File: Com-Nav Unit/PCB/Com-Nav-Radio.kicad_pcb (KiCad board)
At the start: 2 copper layers, 147 x 45 mm, 84 parts, among them J1 GT-USB-7055, Q10 SS8550, Q11 SS8550, Q12 SS8550, Q13 SS8550, Q14 SS8550, Q15 SS8550, Q16 SS8550, Q2 SS8550, Q3 SS8550, Q4 SS8550, Q5 SS8550, Q6 SS8550, Q7 SS8550, Q8 SS8550, Q9 SS8550, SW1 EC12D1524403, SW2 EC12E1240301, SW3 EC12D1524403, SW4 EC12E1240301, U1 STM32F411CEUx, U10 FJ2352BH, U11 FJ2352BH, U12 FJ2352BH, U13 FJ2352BH, U14 FJ2352BH, U2 74HC595, U3 74HC595, U4 XC6206P332MR, U5 FJ2352BH, U6 FJ2352BH, U7 FJ2352BH, U8 FJ2352BH, U9 FJ2352BH, Y2 25 MHz

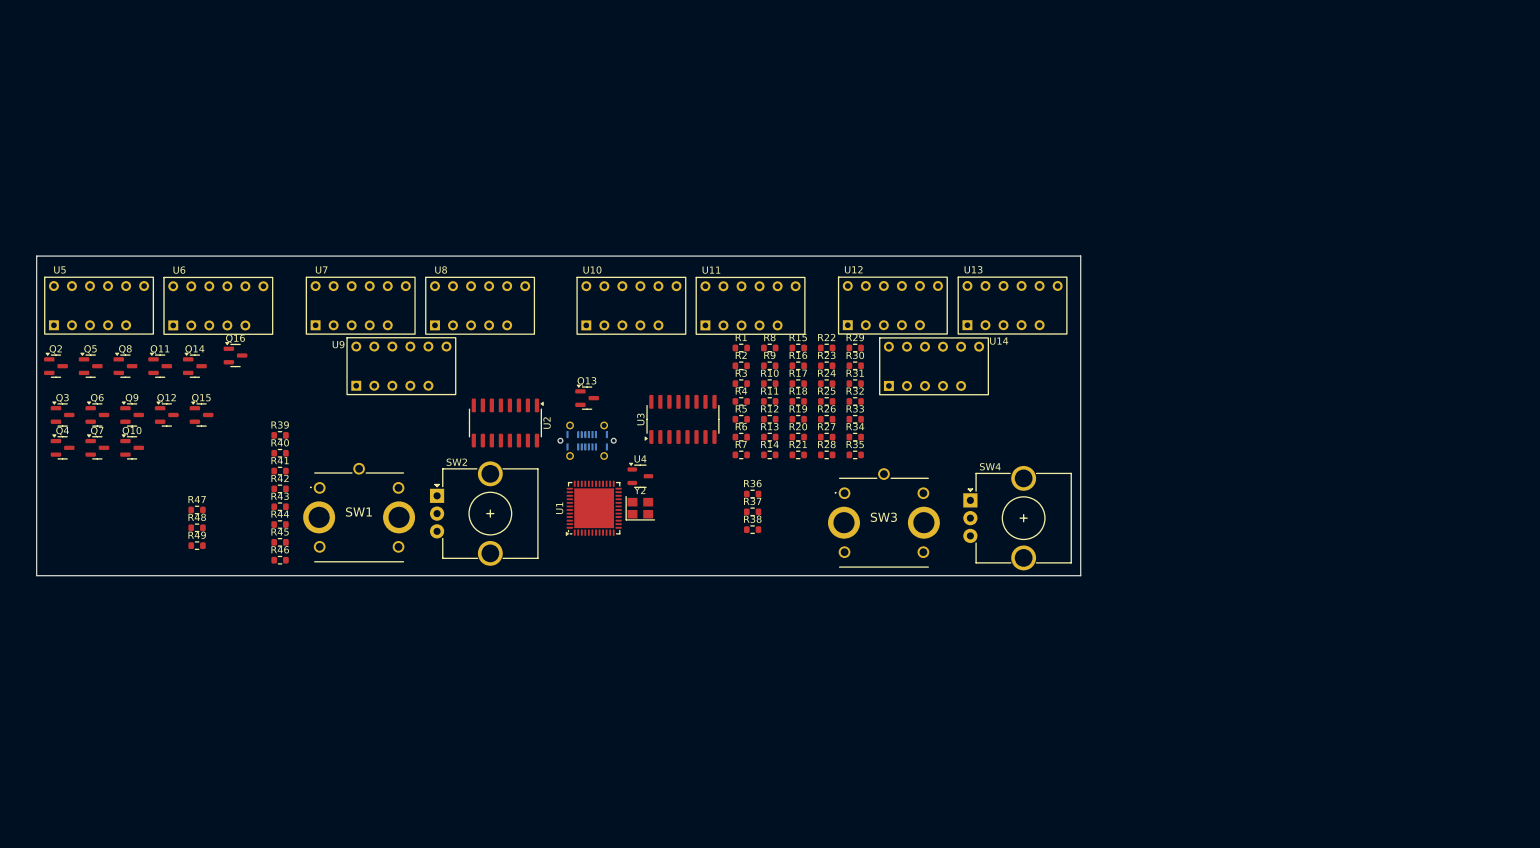
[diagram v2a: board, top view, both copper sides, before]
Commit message: PCB - Changed to common cathode with 2 more shift reg
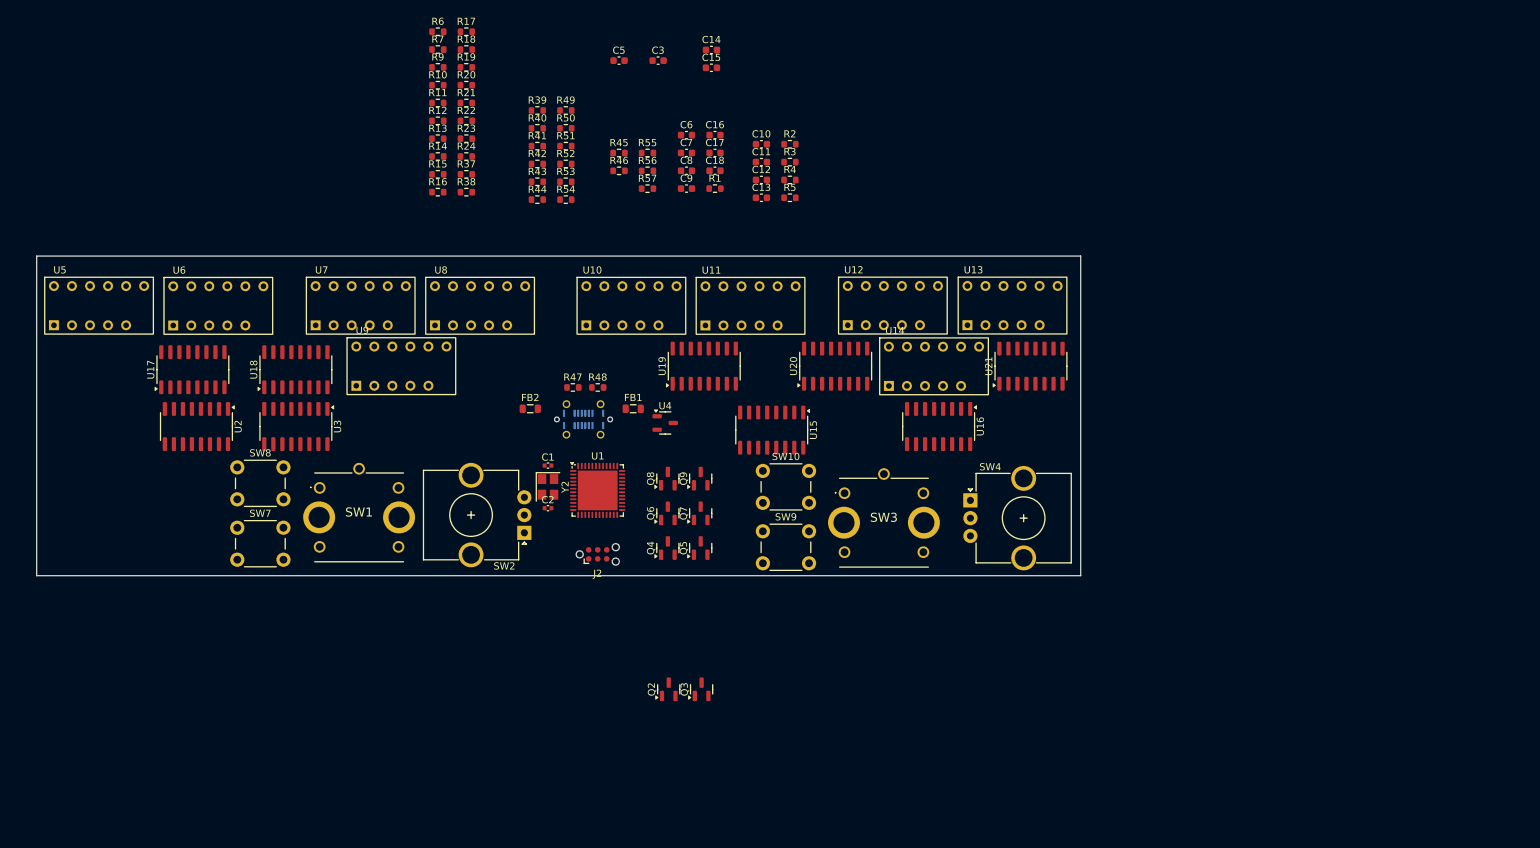
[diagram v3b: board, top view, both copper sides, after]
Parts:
- removed Q10, Q11, Q12, Q13, Q14, Q15, Q16: SS8550, Package_TO_SOT_SMD:SOT-23
- removed R25, R26, R27, R28, R29, R30, R31, R32, R33, R34, R35: 100, Resistor_SMD:R_0603_1608Metric
- removed R36: 0, Resistor_SMD:R_0603_1608Metric
- removed R8: 10k, Resistor_SMD:R_0603_1608Metric
- added C1: 10p, Capacitor_SMD:C_0402_1005Metric, F.Cu at (150.5, 106.5)
- added C10: 100n, Capacitor_SMD:C_0603_1608Metric, F.Cu at (180.6, 61.3)
- added C11: 100n, Capacitor_SMD:C_0603_1608Metric, F.Cu at (180.6, 63.8)
- added C12: 100n, Capacitor_SMD:C_0603_1608Metric, F.Cu at (180.6, 66.3)
- added C13: 100n, Capacitor_SMD:C_0603_1608Metric, F.Cu at (180.6, 68.8)
- added C14: 2.2u, Capacitor_SMD:C_0603_1608Metric, F.Cu at (173.5, 48.0)
- added C15: 100n, Capacitor_SMD:C_0603_1608Metric, F.Cu at (173.5, 50.5)
- added C16: 100n, Capacitor_SMD:C_0603_1608Metric, F.Cu at (174.0, 60.0)
- added C17: 2.2u, Capacitor_SMD:C_0603_1608Metric, F.Cu at (174.0, 62.5)
- added C18: 2.2u, Capacitor_SMD:C_0603_1608Metric, F.Cu at (174.0, 65.0)
- added C2: 10p, Capacitor_SMD:C_0402_1005Metric, F.Cu at (150.5, 112.5)
- added C3: 2.2u, Capacitor_SMD:C_0603_1608Metric, F.Cu at (166.0, 49.5)
- added C5: 2.2u, Capacitor_SMD:C_0603_1608Metric, F.Cu at (160.5, 49.5)
- added C6: 100n, Capacitor_SMD:C_0603_1608Metric, F.Cu at (170.0, 60.0)
- added C7: 2.2u, Capacitor_SMD:C_0603_1608Metric, F.Cu at (170.0, 62.5)
- added C8: 100n, Capacitor_SMD:C_0603_1608Metric, F.Cu at (170.0, 65.0)
- added C9: 100n, Capacitor_SMD:C_0603_1608Metric, F.Cu at (170.0, 67.5)
- added FB1: GZ2012D601TF, Inductor_SMD:L_0805_2012Metric, F.Cu at (162.5, 98.5)
- added FB2: GZ2012D601TF, Inductor_SMD:L_0805_2012Metric, F.Cu at (148.0, 98.5)
- added J2: TC2030, Connector:Tag-Connect_TC2030-IDC-NL_2x03_P1.27mm_Vertical, F.Cu at (157.5, 119.0)
- added R50: 10k, Resistor_SMD:R_0603_1608Metric, F.Cu at (153.0, 59.0)
- added R51: 10k, Resistor_SMD:R_0603_1608Metric, F.Cu at (153.0, 61.5)
- added R52: 10k, Resistor_SMD:R_0603_1608Metric, F.Cu at (153.0, 64.0)
- added R53: 10k, Resistor_SMD:R_0603_1608Metric, F.Cu at (153.0, 66.5)
- added R54: 10k, Resistor_SMD:R_0603_1608Metric, F.Cu at (153.0, 69.0)
- added R55: 10k, Resistor_SMD:R_0603_1608Metric, F.Cu at (164.5, 62.5)
- added R56: 10k, Resistor_SMD:R_0603_1608Metric, F.Cu at (164.5, 65.0)
- added R57: 10k, Resistor_SMD:R_0603_1608Metric, F.Cu at (164.5, 67.5)
- added SW10: SW_Push, Button_Switch_THT:SW_PUSH_6mm, F.Cu at (180.8, 107.2)
- added SW7: SW_Push, Button_Switch_THT:SW_PUSH_6mm, F.Cu at (106.8, 115.2)
- added SW8: SW_Push, Button_Switch_THT:SW_PUSH_6mm, F.Cu at (106.8, 106.8)
- added SW9: SW_Push, Button_Switch_THT:SW_PUSH_6mm, F.Cu at (180.8, 115.8)
- added U15: 74HC595, Package_SO:SOIC-16_3.9x9.9mm_P1.27mm, F.Cu at (182.0, 101.5)
- added U16: 74HC595, Package_SO:SOIC-16_3.9x9.9mm_P1.27mm, F.Cu at (205.5, 101.0)
- added U17: ULN2003A, Package_SO:SOIC-16_3.9x9.9mm_P1.27mm, F.Cu at (100.5, 93.0)
- added U18: ULN2003A, Package_SO:SOIC-16_3.9x9.9mm_P1.27mm, F.Cu at (115.0, 93.0)
- added U19: ULN2003A, Package_SO:SOIC-16_3.9x9.9mm_P1.27mm, F.Cu at (172.5, 92.5)
- added U20: ULN2003A, Package_SO:SOIC-16_3.9x9.9mm_P1.27mm, F.Cu at (191.0, 92.5)
- added U21: ULN2003A, Package_SO:SOIC-16_3.9x9.9mm_P1.27mm, F.Cu at (218.5, 92.5)
- Q2, Q3, Q4, Q5, Q6, Q7, Q8, Q9: value SS8550 -> AO3401A
- R10, R11, R12, R13, R14, R15, R16, R17, R18, R19, R20, R9: value 10k -> 100
- U10, U11, U12, U13, U14, U5, U6, U7, U8, U9: value FJ2352BH -> FJ2352; footprint Custom_7seg:FJ2352BH -> Custom_7seg:FJ2352
- moved Q3 97.9 mm to (172.1, 138.0), turned to 90 degrees
- moved Q2 97.5 mm to (167.5, 138.0), turned to 90 degrees
- moved Q5 89.6 mm to (172.0, 118.1), turned to 90 degrees
- moved Q4 86.4 mm to (167.4, 118.1), turned to 90 degrees
- moved Q7 85.5 mm to (172.0, 113.2), turned to 90 degrees
- moved Q6 81.5 mm to (167.4, 113.2), turned to 90 degrees
- moved Q9 80.6 mm to (172.0, 108.3), turned to 90 degrees
- moved R49 80.3 mm to (153.0, 56.5)
- moved Q8 78.0 mm to (167.4, 108.3), turned to 90 degrees
- moved R45 72.7 mm to (160.5, 62.5)
- moved R46 72.7 mm to (160.5, 65.0)
- moved R6 71.3 mm to (135.0, 45.4)
- moved R7 71.3 mm to (135.0, 47.9)
- moved R19 68.1 mm to (139.0, 50.4)
- moved R17 68.1 mm to (139.0, 45.4)
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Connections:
- J1 pad A4: +5V -> Net-(FB1-Pad1)
- J1 pad A9: +5V -> Net-(FB1-Pad1)
- J1 pad B4: +5V -> Net-(FB1-Pad1)
- J1 pad B9: +5V -> Net-(FB1-Pad1)
- Q2 pad 1: Net-(Q2-B) -> Net-(Q2-G)
- Q2 pad 2: +5V -> Net-(Q2-S)
- Q2 pad 3: /DIG.1 -> Net-(Q2-D)
- Q3 pad 1: Net-(Q3-B) -> Net-(Q3-G)
- Q3 pad 2: +5V -> Net-(Q2-S)
- Q3 pad 3: /DIG2 -> Net-(Q3-D)
- Q4 pad 1: Net-(Q4-B) -> Net-(Q4-G)
- Q4 pad 2: +5V -> Net-(Q2-S)
- Q4 pad 3: /DIG3 -> Net-(Q4-D)
- Q5 pad 1: Net-(Q5-B) -> Net-(Q5-G)
- Q5 pad 2: +5V -> Net-(Q2-S)
- Q5 pad 3: /DIG4 -> Net-(Q5-D)
- Q6 pad 1: Net-(Q6-B) -> Net-(Q6-G)
- Q6 pad 2: +5V -> Net-(Q2-S)
- Q6 pad 3: /DIG5 -> Net-(Q6-D)
- Q7 pad 1: Net-(Q7-B) -> Net-(Q7-G)
- Q7 pad 2: +5V -> Net-(Q2-S)
- Q7 pad 3: /DIG6 -> Net-(Q7-D)
- Q8 pad 1: Net-(Q8-B) -> Net-(Q8-G)
- Q8 pad 2: +5V -> Net-(Q2-S)
- Q8 pad 3: /DIG7 -> Net-(Q8-D)
- Q9 pad 1: Net-(Q9-B) -> Net-(Q9-G)
- Q9 pad 2: +5V -> Net-(Q2-S)
- Q9 pad 3: /DIG8 -> Net-(Q9-D)
- R10 pad 1: Net-(Q6-B) -> unconnected-(R10-Pad1)
- R10 pad 2: Net-(U2-QE) -> Net-(Q2-G)
- R11 pad 1: Net-(Q7-B) -> unconnected-(R11-Pad1)
- R11 pad 2: Net-(U2-QF) -> Net-(Q3-G)
- R12 pad 1: Net-(Q8-B) -> unconnected-(R12-Pad1)
- R12 pad 2: Net-(U2-QG) -> Net-(Q4-G)
- R13 pad 1: Net-(Q9-B) -> unconnected-(R13-Pad1)
- R13 pad 2: Net-(U2-QH) -> Net-(Q5-G)
- R14 pad 1: Net-(Q10-B) -> unconnected-(R14-Pad1)
- R14 pad 2: Net-(U3-QA) -> Net-(Q6-G)
- R15 pad 1: Net-(Q11-B) -> unconnected-(R15-Pad1)
- R15 pad 2: Net-(U3-QB) -> Net-(Q7-G)
- R16 pad 1: Net-(Q12-B) -> unconnected-(R16-Pad1)
- R16 pad 2: Net-(U3-QC) -> Net-(Q8-G)
- R17 pad 1: Net-(Q13-B) -> unconnected-(R17-Pad1)
- R17 pad 2: Net-(U3-QD) -> Net-(Q9-G)
- R18 pad 1: Net-(Q14-B) -> Net-(Q3-D)
- R18 pad 2: Net-(U3-QE) -> /SEG2
- R19 pad 1: Net-(Q15-B) -> Net-(Q4-D)
- R19 pad 2: Net-(U3-QF) -> /SEG3
- R20 pad 1: Net-(Q16-B) -> Net-(Q5-D)
- R20 pad 2: Net-(U3-QG) -> /SEG4
- R21 pad 1: Net-(U1-PB0) -> Net-(Q6-D)
- R21 pad 2: /SEG1_1 -> /SEG5
- R22 pad 1: Net-(U1-PB1) -> Net-(Q7-D)
- R22 pad 2: /SEG1_2 -> /SEG6
- R23 pad 1: Net-(U1-PB2) -> Net-(Q8-D)
- R23 pad 2: /SEG1_3 -> /SEG7
- R24 pad 1: Net-(U1-PB3) -> Net-(Q9-D)
- R24 pad 2: /SEG1_4 -> /SEG8
- R37 pad 2: /SEG1_3 -> Net-(U1-PB2)
- R43 pad 2: /ENC1_A -> /ENC3_A
- R44 pad 2: /ENC1_B -> /ENC3_B
- R45 pad 2: /ENC2_A -> /ENC4_A
- R46 pad 2: /ENC2_B -> /ENC4_B
- R6 pad 1: Net-(Q2-B) -> Net-(U15-~{SRCLR})
- R6 pad 2: Net-(U2-QA) -> +5V
- R7 pad 1: Net-(Q3-B) -> Net-(U16-~{SRCLR})
- R7 pad 2: Net-(U2-QB) -> +5V
- R9 pad 1: Net-(Q5-B) -> Net-(Q2-D)
- R9 pad 2: Net-(U2-QD) -> /SEG1
- SW3 pad A: /ENC1_A -> /ENC3_A
- SW3 pad B: /ENC1_B -> /ENC3_B
- SW4 pad A: /ENC2_A -> /ENC4_A
- SW4 pad B: /ENC2_B -> /ENC4_B
- U1 pad 10: unconnected-(U1-PA0-Pad10) -> /ENC1_A
- U1 pad 11: unconnected-(U1-PA1-Pad11) -> /ENC1_B
- U1 pad 12: unconnected-(U1-PA2-Pad12) -> /ENC2_A
- U1 pad 13: unconnected-(U1-PA3-Pad13) -> /ENC2_B
- U1 pad 14: unconnected-(U1-PA4-Pad14) -> /ENC3_A
- U1 pad 18: Net-(U1-PB0) -> unconnected-(U1-PB0-Pad18)
- U1 pad 19: Net-(U1-PB1) -> unconnected-(U1-PB1-Pad19)
- U1 pad 2: /SEG2_8 -> unconnected-(U1-PC13-Pad2)
- U1 pad 21: Net-(U1-PB10) -> unconnected-(U1-PB10-Pad21)
- U1 pad 25: Net-(U1-PB12) -> unconnected-(U1-PB12-Pad25)
- U1 pad 26: Net-(U1-PB13) -> unconnected-(U1-PB13-Pad26)
- U1 pad 27: Net-(U1-PB14) -> unconnected-(U1-PB14-Pad27)
- U1 pad 28: Net-(U1-PB15) -> unconnected-(U1-PB15-Pad28)
- U1 pad 29: unconnected-(U1-PA8-Pad29) -> /ENC3_B
- U1 pad 30: unconnected-(U1-PA9-Pad30) -> /ENC4_A
- U1 pad 31: unconnected-(U1-PA10-Pad31) -> /ENC4_B
- U1 pad 34: unconnected-(U1-PA13-Pad34) -> /SWDIO
- U1 pad 37: unconnected-(U1-PA14-Pad37) -> /SWDCLK
- U1 pad 39: Net-(U1-PB3) -> /SWO
- U1 pad 40: Net-(U1-PB4) -> unconnected-(U1-PB4-Pad40)
- U1 pad 41: Net-(U1-PB5) -> unconnected-(U1-PB5-Pad41)
- U1 pad 42: Net-(U1-PB6) -> unconnected-(U1-PB6-Pad42)
- U1 pad 43: Net-(U1-PB7) -> unconnected-(U1-PB7-Pad43)
- U1 pad 45: Net-(U1-PB8) -> unconnected-(U1-PB8-Pad45)
- U1 pad 46: Net-(U1-PB9) -> unconnected-(U1-PB9-Pad46)
- U10 pad 1: /SEG2_5 -> /SEG5
- U10 pad 10: /SEG2_6 -> /SEG6
- U10 pad 11: /SEG2_1 -> /SEG1
- U10 pad 12: /DIG1 -> /DIG16
- U10 pad 2: /SEG2_4 -> /SEG4
- U10 pad 3: /SEG2_8 -> /SEG8
- U10 pad 4: /SEG2_3 -> /SEG3
- U10 pad 5: /SEG2_7 -> /SEG7
- U10 pad 7: /SEG2_2 -> /SEG2
- U10 pad 8: /DIG3 -> /DIG18
- U10 pad 9: /DIG2 -> /DIG17
- U11 pad 1: /SEG2_5 -> /SEG5
- U11 pad 10: /SEG2_6 -> /SEG6
- U11 pad 11: /SEG2_1 -> /SEG1
- U11 pad 12: /DIG4 -> /DIG19
- U11 pad 2: /SEG2_4 -> /SEG4
- U11 pad 3: /SEG2_8 -> /SEG8
- U11 pad 4: /SEG2_3 -> /SEG3
- U11 pad 5: /SEG2_7 -> /SEG7
- U11 pad 7: /SEG2_2 -> /SEG2
- U11 pad 8: /DIG6 -> /DIG21
- U11 pad 9: /DIG5 -> /DIG20
- U12 pad 1: /SEG2_5 -> /SEG5
- U12 pad 10: /SEG2_6 -> /SEG6
- U12 pad 11: /SEG2_1 -> /SEG1
- U12 pad 12: /DIG7 -> /DIG22
- U12 pad 2: /SEG2_4 -> /SEG4
- U12 pad 3: /SEG2_8 -> /SEG8
- U12 pad 4: /SEG2_3 -> /SEG3
- U12 pad 5: /SEG2_7 -> /SEG7
- U12 pad 7: /SEG2_2 -> /SEG2
- U12 pad 8: /DIG9 -> /DIG24
- U12 pad 9: /DIG8 -> /DIG23
- U13 pad 1: /SEG2_5 -> /SEG5
- U13 pad 10: /SEG2_6 -> /SEG6
- U13 pad 11: /SEG2_1 -> /SEG1
- U13 pad 12: /DIG13 -> /DIG28
- U13 pad 2: /SEG2_4 -> /SEG4
- U13 pad 3: /SEG2_8 -> /SEG8
- U13 pad 4: /SEG2_3 -> /SEG3
- U13 pad 5: /SEG2_7 -> /SEG7
- U13 pad 7: /SEG2_2 -> /SEG2
- U13 pad 8: /DIG15 -> /DIG30
- U13 pad 9: /DIG14 -> /DIG29
- U14 pad 1: /SEG2_5 -> /SEG5
- U14 pad 10: /SEG2_6 -> /SEG6
- U14 pad 11: /SEG2_1 -> /SEG1
- U14 pad 12: /DIG10 -> /DIG25
- U14 pad 2: /SEG2_4 -> /SEG4
- U14 pad 3: /SEG2_8 -> /SEG8
- U14 pad 4: /SEG2_3 -> /SEG3
- U14 pad 5: /SEG2_7 -> /SEG7
- U14 pad 7: /SEG2_2 -> /SEG2
- U14 pad 8: /DIG12 -> /DIG27
- U14 pad 9: /DIG11 -> /DIG26
- U2 pad 1: Net-(U2-QB) -> Net-(U17-I2)
- U2 pad 15: Net-(U2-QA) -> Net-(U17-I1)
- U2 pad 16: +5V -> +3.3V
- U2 pad 3: Net-(U2-QD) -> Net-(U17-I4)
- U2 pad 4: Net-(U2-QE) -> Net-(U17-I5)
- U2 pad 5: Net-(U2-QF) -> Net-(U17-I6)
- U2 pad 6: Net-(U2-QG) -> Net-(U17-I7)
- U2 pad 7: Net-(U2-QH) -> Net-(U18-I1)
- U3 pad 1: Net-(U3-QB) -> Net-(U18-I3)
- U3 pad 15: Net-(U3-QA) -> Net-(U18-I2)
- U3 pad 16: +5V -> +3.3V
- U3 pad 2: Net-(U3-QC) -> Net-(U18-I4)
- U3 pad 3: Net-(U3-QD) -> Net-(U18-I5)
- U3 pad 4: Net-(U3-QE) -> Net-(U18-I6)
- U3 pad 5: Net-(U3-QF) -> Net-(U18-I7)
- U3 pad 6: Net-(U3-QG) -> Net-(U19-I1)
- U3 pad 7: unconnected-(U3-QH-Pad7) -> Net-(U19-I2)
- U3 pad 9: unconnected-(U3-QH'-Pad9) -> Net-(U15-SER)
- U5 pad 1: /SEG1_5 -> /SEG5
- U5 pad 10: /SEG1_6 -> /SEG6
- U5 pad 11: /SEG1_1 -> /SEG1
- U5 pad 2: /SEG1_4 -> /SEG4
- U5 pad 3: /SEG1_8 -> /SEG8
- U5 pad 4: /SEG1_3 -> /SEG3
- U5 pad 5: /SEG1_7 -> /SEG7
- U5 pad 7: /SEG1_2 -> /SEG2
- U6 pad 1: /SEG1_5 -> /SEG5
- U6 pad 10: /SEG1_6 -> /SEG6
- U6 pad 11: /SEG1_1 -> /SEG1
- U6 pad 2: /SEG1_4 -> /SEG4
- U6 pad 3: /SEG1_8 -> /SEG8
- U6 pad 4: /SEG1_3 -> /SEG3
- U6 pad 5: /SEG1_7 -> /SEG7
- U6 pad 7: /SEG1_2 -> /SEG2
- U7 pad 1: /SEG1_5 -> /SEG5
- U7 pad 10: /SEG1_6 -> /SEG6
- U7 pad 11: /SEG1_1 -> /SEG1
- U7 pad 2: /SEG1_4 -> /SEG4
- U7 pad 3: /SEG1_8 -> /SEG8
- U7 pad 4: /SEG1_3 -> /SEG3
- U7 pad 5: /SEG1_7 -> /SEG7
- U7 pad 7: /SEG1_2 -> /SEG2
- U8 pad 1: /SEG1_5 -> /SEG5
- U8 pad 10: /SEG1_6 -> /SEG6
- U8 pad 11: /SEG1_1 -> /SEG1
- U8 pad 2: /SEG1_4 -> /SEG4
- U8 pad 3: /SEG1_8 -> /SEG8
- U8 pad 4: /SEG1_3 -> /SEG3
- U8 pad 5: /SEG1_7 -> /SEG7
- U8 pad 7: /SEG1_2 -> /SEG2
- U9 pad 1: /SEG1_5 -> /SEG5
- U9 pad 10: /SEG1_6 -> /SEG6
- U9 pad 11: /SEG1_1 -> /SEG1
- U9 pad 2: /SEG1_4 -> /SEG4
- U9 pad 3: /SEG1_8 -> /SEG8
- U9 pad 4: /SEG1_3 -> /SEG3
- U9 pad 5: /SEG1_7 -> /SEG7
- U9 pad 7: /SEG1_2 -> /SEG2
- Y2 pad 1: Net-(U1-PH1) -> Net-(U1-PH0)
- Y2 pad 3: Net-(U1-PH0) -> Net-(U1-PH1)

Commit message: PCB - Add swd connector, add switches
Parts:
- removed the SW1 at (123.9, 113.8)
- removed the SW3 at (197.8, 114.5)
- added D1: 1N4148WS, Diode_SMD:D_SOD-323, F.Cu at (114.8, 48.8)
- added D2: 1N4148WS, Diode_SMD:D_SOD-323, F.Cu at (114.8, 52.1)
- added D3: 1N4148WS, Diode_SMD:D_SOD-323, F.Cu at (114.8, 55.5)
- added D4: 1N4148WS, Diode_SMD:D_SOD-323, F.Cu at (114.8, 58.8)
- added D5: 1N4148WS, Diode_SMD:D_SOD-323, F.Cu at (114.8, 62.1)
- added D6: 1N4148WS, Diode_SMD:D_SOD-323, F.Cu at (114.8, 65.5)
- added J2: Conn_02x05_Odd_Even, Connector_PinHeader_1.27mm:PinHeader_2x05_P1.27mm_Vertical_SMD, B.Cu at (126.5, 100.5)
- added J5: Conn_01x03, Connector_PinSocket_2.54mm:PinSocket_1x03_P2.54mm_Horizontal, F.Cu at (287.0, 75.8)
- added Q9: AO3401A, Package_TO_SOT_SMD:SOT-23, F.Cu at (119.9, 57.0)
- added R30: 10k, Resistor_SMD:R_0603_1608Metric, F.Cu at (119.5, 53.4)
- added R35: 100, Resistor_SMD:R_0603_1608Metric, F.Cu at (119.5, 50.8)
- added R43: 10k, Resistor_SMD:R_0603_1608Metric, F.Cu at (119.5, 48.3)
- added SW2: EC12D1524403, Encoder:EC12D1524403, F.Cu at (266.5, 82.7)
- added SW7: EC12D1524403, Encoder:EC12D1524403, F.Cu at (266.5, 99.7)
- added U23: USBLC6-2SC6, Package_TO_SOT_SMD:SOT-23-6, F.Cu at (278.5, 94.0)
- J2: moved to B.Cu
- moved J2 32.3 mm to (127.0, 108.2), turned to 180 degrees
- moved Q3 26.2 mm to (152.2, 139.5)
- moved Q4 26.2 mm to (156.9, 139.5)
- moved Q7 26.2 mm to (152.2, 129.8)
- moved Q8 26.2 mm to (156.9, 129.8)
- moved Q5 26.2 mm to (152.2, 134.6)
- moved Q6 26.2 mm to (156.9, 134.6)
- moved SW5 8.02 mm to (188.8, 115.2)
- moved SW6 8.02 mm to (188.8, 106.8)
- moved SW3 3.29 mm to (110.0, 114.8)
- moved SW4 3.29 mm to (110.0, 106.2)
- renumbered C5 to C1, C16 to C14, C8 to C15, C9 to C16, C15 to C17, C14 to C2, C6 to C3, C17 to C4, C18 to C5, C7 to C6, C2 to C7, C1 to C8, C3 to C9, Q2 to Q1, Q3 to Q2, Q4 to Q3, Q5 to Q4, Q6 to Q5, Q7 to Q6, Q8 to Q7, Q9 to Q8, R49 to R1, R48 to R10, R47 to R11, R50 to R12, R51 to R13, R52 to R14, R53 to R15, R54 to R16, R55 to R17, R56 to R18, R57 to R19, R9 to R2, R10 to R20, R11 to R21, R12 to R22, R13 to R23, R14 to R24, R15 to R25, R16 to R26, R17 to R27, R45 to R28, R46 to R29, R18 to R3, R43 to R31, R44 to R32, R37 to R33, R38 to R34, R41 to R36, R42 to R37, R3 to R38, R4 to R39, R19 to R4, R5 to R40, R40 to R41, R39 to R42, R1 to R44, R2 to R45, R6 to R46, R7 to R47, R20 to R5, R21 to R6, R22 to R7, R23 to R8, R24 to R9, SW4 to SW1, SW7 to SW3, SW8 to SW4, SW9 to SW5, SW10 to SW6, SW2 to SW8, U10 to U1, U13 to U10, U9 to U11, U1 to U12, U2 to U13, U3 to U14, U5 to U2, U11 to U3, U6 to U4, U12 to U5, U7 to U6, U14 to U7, U4 to U9, Y2 to Y1
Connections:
- net /BOOT0 renamed Net-(U12-BOOT0)
- C1 pad 1: +5V -> unconnected-(C1-Pad1)
- C1 pad 2: GND -> Net-(C1-Pad2)
- C2 pad 1: Net-(Q2-S) -> unconnected-(C2-Pad1)
- C2 pad 2: GND -> Net-(C2-Pad2)
- C3 pad 1: +5V -> unconnected-(C3-Pad1)
- C3 pad 2: GND -> unconnected-(C3-Pad2)
- C4 pad 1: Net-(Q2-S) -> unconnected-(C4-Pad1)
- C5 pad 1: Net-(Q2-S) -> Net-(C5-Pad1)
- C5 pad 2: GND -> Net-(C2-Pad2)
- C6 pad 2: GND -> Net-(C1-Pad2)
- C7 pad 1: Net-(U1-PH0) -> Net-(U12-PH0)
- C7 pad 2: GND -> Net-(C7-Pad2)
- C8 pad 1: Net-(U1-PH1) -> Net-(U12-PH1)
- C8 pad 2: GND -> Net-(C7-Pad2)
- FB1 pad 1: Net-(FB1-Pad1) -> Net-(U23-VBUS)
- FB1 pad 2: +5V -> Net-(U9-VI)
- FB2 pad 1: Net-(FB1-Pad1) -> unconnected-(FB2-Pad1)
- FB2 pad 2: Net-(Q2-S) -> Net-(C5-Pad1)
- J1 pad A4: Net-(FB1-Pad1) -> Net-(U23-VBUS)
- J1 pad A6: /USB_D- -> Net-(J1-D+-PadA6)
- J1 pad A7: /USB_D+ -> Net-(J1-D--PadA7)
- J1 pad A9: Net-(FB1-Pad1) -> Net-(U23-VBUS)
- J1 pad B4: Net-(FB1-Pad1) -> Net-(U23-VBUS)
- J1 pad B6: /USB_D- -> Net-(J1-D+-PadA6)
- J1 pad B7: /USB_D+ -> Net-(J1-D--PadA7)
- J1 pad B9: Net-(FB1-Pad1) -> Net-(U23-VBUS)
- Q1 pad 1: Net-(Q2-G) -> Net-(Q1-G)
- Q1 pad 2: Net-(Q2-S) -> unconnected-(Q1-S-Pad2)
- Q2 pad 1: Net-(Q3-G) -> Net-(Q2-G)
- Q2 pad 2: Net-(Q2-S) -> unconnected-(Q2-S-Pad2)
- Q3 pad 1: Net-(Q4-G) -> Net-(Q3-G)
- Q3 pad 2: Net-(Q2-S) -> unconnected-(Q3-S-Pad2)
- Q4 pad 1: Net-(Q5-G) -> Net-(Q4-G)
- Q4 pad 2: Net-(Q2-S) -> unconnected-(Q4-S-Pad2)
- Q5 pad 1: Net-(Q6-G) -> Net-(Q5-G)
- Q5 pad 2: Net-(Q2-S) -> unconnected-(Q5-S-Pad2)
- Q6 pad 1: Net-(Q7-G) -> Net-(Q6-G)
- Q6 pad 2: Net-(Q2-S) -> unconnected-(Q6-S-Pad2)
- Q7 pad 1: Net-(Q8-G) -> Net-(Q7-G)
- Q7 pad 2: Net-(Q2-S) -> unconnected-(Q7-S-Pad2)
- Q8 pad 1: Net-(Q9-G) -> Net-(Q8-G)
- Q8 pad 2: Net-(Q2-S) -> unconnected-(Q8-S-Pad2)
- R1 pad 2: GND -> unconnected-(R1-Pad2)
- R10 pad 2: GND -> Net-(R10-Pad2)
- R11 pad 2: GND -> Net-(R10-Pad2)
- R12 pad 1: Net-(Q2-G) -> unconnected-(R12-Pad1)
- R12 pad 2: Net-(Q2-S) -> unconnected-(R12-Pad2)
- R13 pad 1: Net-(Q3-G) -> unconnected-(R13-Pad1)
- R13 pad 2: Net-(Q2-S) -> unconnected-(R13-Pad2)
- R14 pad 1: Net-(Q4-G) -> unconnected-(R14-Pad1)
- R14 pad 2: Net-(Q2-S) -> unconnected-(R14-Pad2)
- R15 pad 1: Net-(Q5-G) -> unconnected-(R15-Pad1)
- R15 pad 2: Net-(Q2-S) -> unconnected-(R15-Pad2)
- R16 pad 1: Net-(Q6-G) -> unconnected-(R16-Pad1)
- R16 pad 2: Net-(Q2-S) -> unconnected-(R16-Pad2)
- R17 pad 1: Net-(Q7-G) -> unconnected-(R17-Pad1)
- R17 pad 2: Net-(Q2-S) -> unconnected-(R17-Pad2)
- R18 pad 1: Net-(Q8-G) -> unconnected-(R18-Pad1)
- R18 pad 2: Net-(Q2-S) -> unconnected-(R18-Pad2)
- R19 pad 1: Net-(Q9-G) -> unconnected-(R19-Pad1)
- R19 pad 2: Net-(Q2-S) -> unconnected-(R19-Pad2)
- R20 pad 1: unconnected-(R10-Pad1) -> /SEG_CT1
- R20 pad 2: Net-(Q2-G) -> Net-(Q1-G)
- R21 pad 1: unconnected-(R11-Pad1) -> /SEG_CT2
- R21 pad 2: Net-(Q3-G) -> Net-(Q2-G)
- R22 pad 1: unconnected-(R12-Pad1) -> /SEG_CT3
- R22 pad 2: Net-(Q4-G) -> Net-(Q3-G)
- R23 pad 1: unconnected-(R13-Pad1) -> /SEG_CT4
- R23 pad 2: Net-(Q5-G) -> Net-(Q4-G)
- R24 pad 1: unconnected-(R14-Pad1) -> /SEG_CT5
- R24 pad 2: Net-(Q6-G) -> Net-(Q5-G)
- R25 pad 1: unconnected-(R15-Pad1) -> /SEG_CT6
- R25 pad 2: Net-(Q7-G) -> Net-(Q6-G)
- R26 pad 1: unconnected-(R16-Pad1) -> /SEG_CT7
- R26 pad 2: Net-(Q8-G) -> Net-(Q7-G)
- R27 pad 1: unconnected-(R17-Pad1) -> /SEG_CT8
- R27 pad 2: Net-(Q9-G) -> Net-(Q8-G)
- R28 pad 1: +3.3V -> Net-(R28-Pad1)
- R29 pad 1: +3.3V -> Net-(R28-Pad1)
- R31 pad 1: +3.3V -> Net-(R31-Pad1)
- R32 pad 1: +3.3V -> Net-(R31-Pad1)
- R36 pad 1: +3.3V -> Net-(R36-Pad1)
- R37 pad 1: +3.3V -> Net-(R36-Pad1)
- R38 pad 2: Net-(U1-PA5) -> Net-(U12-PA2)
- R39 pad 1: Net-(U15-~{OE}) -> unconnected-(R39-Pad1)
- R39 pad 2: Net-(U1-PA6) -> Net-(U12-PA3)
- R40 pad 1: Net-(U15-RCLK) -> Net-(U16-RCLK)
- R40 pad 2: Net-(U1-PA7) -> Net-(U12-PA5)
- R41 pad 1: +3.3V -> Net-(R41-Pad1)
- R42 pad 1: +3.3V -> Net-(R41-Pad1)
- R44 pad 2: +5V -> +3.3V
- R45 pad 2: +5V -> +3.3V
- R46 pad 2: +5V -> +3.3V
- R47 pad 2: +5V -> +3.3V
- SW3 pad 2: unconnected-(SW7-Pad2) -> Net-(D2-K)
- SW4 pad 2: unconnected-(SW8-Pad2) -> Net-(D3-K)
- SW5 pad 1: unconnected-(SW9-Pad1) -> /SW_COM
- SW5 pad 2: unconnected-(SW9-Pad2) -> Net-(D4-K)
- SW6 pad 2: unconnected-(SW10-Pad2) -> Net-(D5-K)
- U12 pad 12: /ENC2_A -> Net-(U12-PA2)
- U12 pad 13: /ENC2_B -> Net-(U12-PA3)
- U12 pad 14: /ENC3_A -> /POT1
- U12 pad 15: Net-(U1-PA5) -> Net-(U12-PA5)
- U12 pad 16: Net-(U1-PA6) -> unconnected-(U12-PA6-Pad16)
- U12 pad 17: Net-(U1-PA7) -> /ENC3_B
- U12 pad 18: unconnected-(U1-PB0-Pad18) -> /SW_COM
- U12 pad 2: unconnected-(U1-PC13-Pad2) -> Net-(U12-PC13)
- U12 pad 21: unconnected-(U1-PB10-Pad21) -> /SEG_CT4
- U12 pad 23: GND -> Net-(U12-VSSA)
- U12 pad 24: +3.3V -> Net-(U12-VDDA)
- U12 pad 25: unconnected-(U1-PB12-Pad25) -> /SEG_CT5
- U12 pad 26: unconnected-(U1-PB13-Pad26) -> /SEG_CT6
- U12 pad 27: unconnected-(U1-PB14-Pad27) -> /SEG_CT7
- U12 pad 28: unconnected-(U1-PB15-Pad28) -> /SEG_CT8
- U12 pad 29: /ENC3_B -> /ENC2_A
- U12 pad 30: /ENC4_A -> /ENC2_B
- U12 pad 31: /ENC4_B -> unconnected-(U12-PA10-Pad31)
- U12 pad 35: GND -> Net-(U12-VSSA)
- U12 pad 40: unconnected-(U1-PB4-Pad40) -> /ENC3_A
- U12 pad 41: unconnected-(U1-PB5-Pad41) -> /SEG_CT1
- U12 pad 42: unconnected-(U1-PB6-Pad42) -> /ENC4_A
- U12 pad 43: unconnected-(U1-PB7-Pad43) -> /ENC4_B
- U12 pad 45: unconnected-(U1-PB8-Pad45) -> /SEG_CT2
- U12 pad 46: unconnected-(U1-PB9-Pad46) -> /SEG_CT3
- U12 pad 47: GND -> Net-(U12-VSSA)
- U12 pad 48: +3.3V -> unconnected-(U12-VDD-Pad48)
- U12 pad 49: GND -> Net-(U12-VSSA)
- U12 pad 5: Net-(U1-PH0) -> Net-(U12-PH0)
- U12 pad 6: Net-(U1-PH1) -> Net-(U12-PH1)
- U12 pad 8: GND -> Net-(U12-VSSA)
- U12 pad 9: +3.3V -> Net-(U12-VDDA)
- U13 pad 11: Net-(U15-RCLK) -> unconnected-(U13-SRCLK-Pad11)
- U13 pad 12: Net-(U15-RCLK) -> unconnected-(U13-RCLK-Pad12)
- U13 pad 13: Net-(U15-~{OE}) -> unconnected-(U13-~{OE}-Pad13)
- U14 pad 11: Net-(U15-RCLK) -> unconnected-(U14-SRCLK-Pad11)
- U14 pad 12: Net-(U15-RCLK) -> unconnected-(U14-RCLK-Pad12)
- U14 pad 13: Net-(U15-~{OE}) -> unconnected-(U14-~{OE}-Pad13)
- U15 pad 12: Net-(U15-RCLK) -> unconnected-(U15-RCLK-Pad12)
- U15 pad 13: Net-(U15-~{OE}) -> unconnected-(U15-~{OE}-Pad13)
- U16 pad 12: Net-(U15-RCLK) -> Net-(U16-RCLK)
- U16 pad 13: Net-(U15-~{OE}) -> Net-(U16-~{OE})
- U21 pad 4: GND -> unconnected-(U21-I4-Pad4)
- U21 pad 5: GND -> unconnected-(U21-I5-Pad5)
- U21 pad 6: GND -> unconnected-(U21-I6-Pad6)
- U21 pad 7: GND -> unconnected-(U21-I7-Pad7)
- U9 pad 3: +5V -> Net-(U9-VI)
- Y1 pad 1: Net-(U1-PH0) -> unconnected-(Y1-Pad1)
- Y1 pad 2: GND -> unconnected-(Y1-Pad2)
- Y1 pad 3: Net-(U1-PH1) -> unconnected-(Y1-Pad3)
